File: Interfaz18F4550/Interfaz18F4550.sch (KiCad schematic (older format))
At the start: 13 parts, among them P1 USB-A, U1 LM7805, U2 PIC18F4550, Y1 Crystal_Small

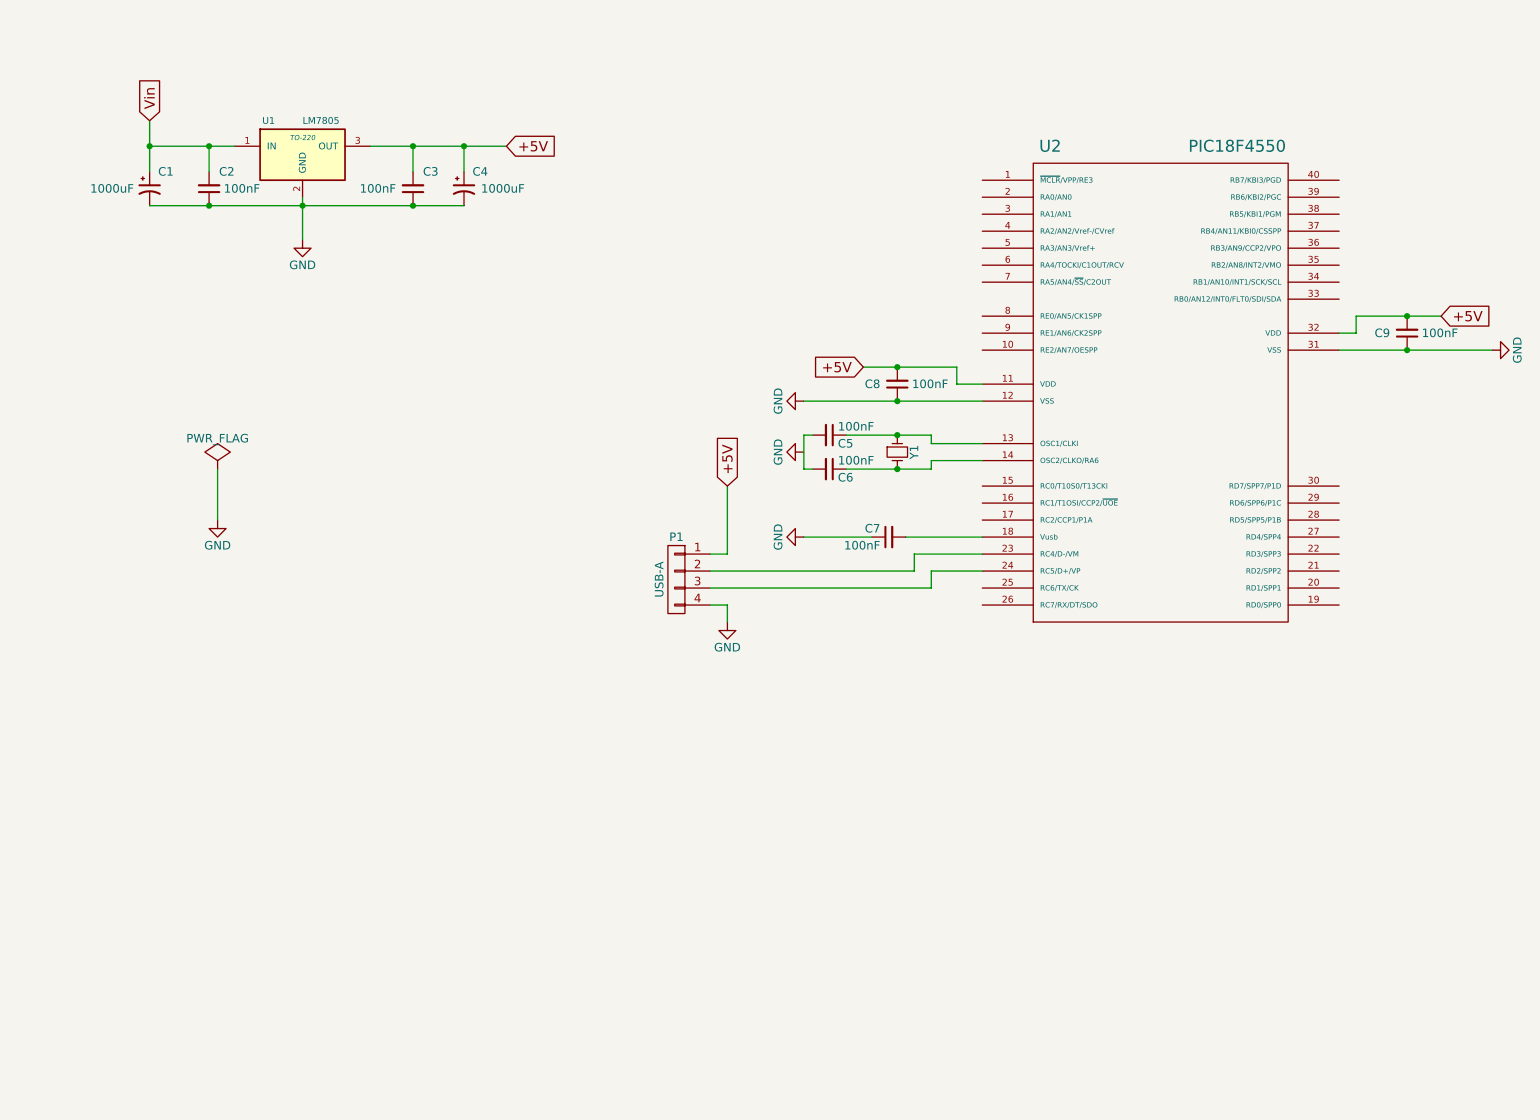
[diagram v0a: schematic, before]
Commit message: Avanzando en interfaz 18f4550
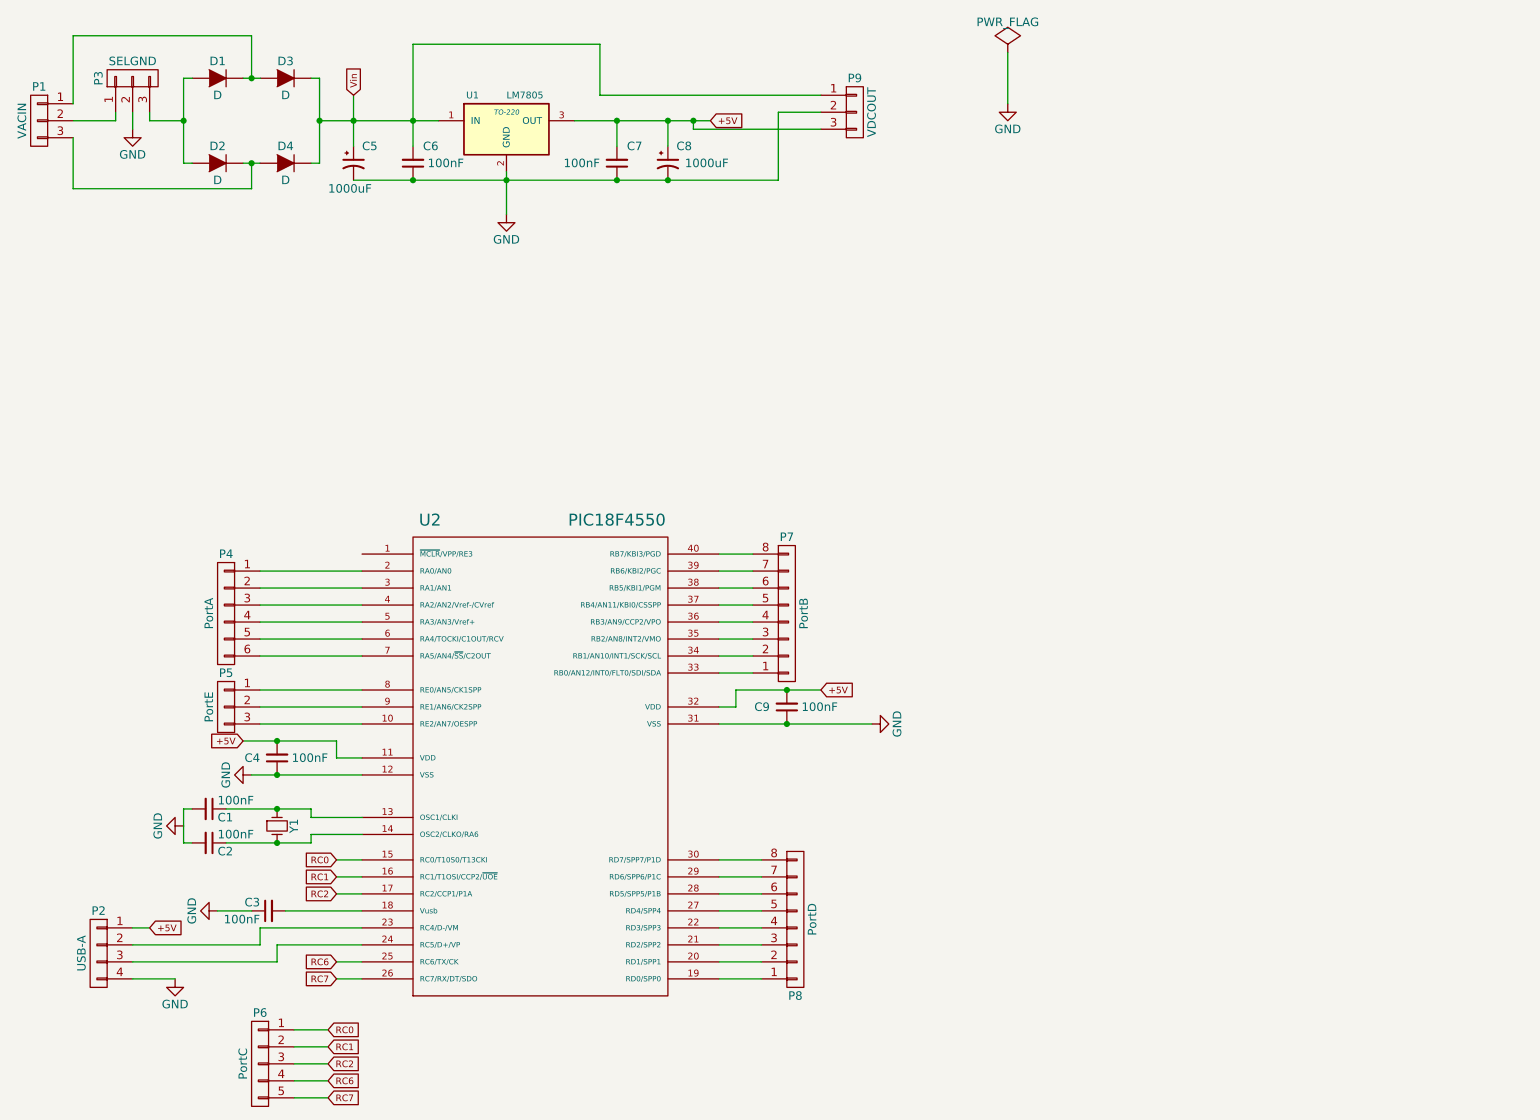
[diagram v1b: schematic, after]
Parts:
- added D1, D2, D3, D4: D, symbol D
- added P1: VACIN, symbol CONN_01X03
- added P3: SELGND, symbol CONN_01X03
- added P4: PortA, symbol CONN_01X06
- added P5: PortE, symbol CONN_01X03
- added P6: PortC, symbol CONN_01X05
- added P7: PortB, symbol CONN_01X08
- added P8: PortD, symbol CONN_01X08
- added P9: VDCOUT, symbol CONN_01X03
- renumbered C5 to C1, C6 to C2, C7 to C3, C8 to C4, C1 to C5, C2 to C6, C3 to C7, C4 to C8, P1 to P2
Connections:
- net +5V: now also P9.3 (P3)
- net GND: now also P3.2 (P2), P9.2 (P2)
- net Vin: now also D3.2 (K), D4.2 (K), P9.1 (P1)
- net at U2.10 (RE2/AN7/OESPP): now also P5.3 (P3)
- net RC0: now reaches U2.15 (RC0/T10S0/T13CKI)
- net RC0: now also P6.1 (P1)
- net RC1: now reaches U2.16 (RC1/T1OSI/CCP2/~UOE~)
- net RC1: now also P6.2 (P2)
- net RC2: now reaches U2.17 (RC2/CCP1/P1A)
- net RC2: now also P6.3 (P3)
- net at U2.19 (RD0/SPP0): now also P8.1 (P1)
- net at U2.2 (RA0/AN0): now also P4.1 (P1)
- net at U2.20 (RD1/SPP1): now also P8.2 (P2)
- net at U2.21 (RD2/SPP2): now also P8.3 (P3)
- net at U2.22 (RD3/SPP3): now also P8.4 (P4)
- net RC6: now reaches U2.25 (RC6/TX/CK)
- net RC6: now also P6.4 (P4)
- net RC7: now reaches U2.26 (RC7/RX/DT/SDO)
- net RC7: now also P6.5 (P5)
- net at U2.27 (RD4/SPP4): now also P8.5 (P5)
- net at U2.28 (RD5/SPP5/P1B): now also P8.6 (P6)
- net at U2.29 (RD6/SPP6/P1C): now also P8.7 (P7)
- net at U2.3 (RA1/AN1): now also P4.2 (P2)
- net at U2.30 (RD7/SPP7/P1D): now also P8.8 (P8)
- net at U2.33 (RB0/AN12/INT0/FLT0/SDI/SDA): now also P7.1 (P1)
- net at U2.34 (RB1/AN10/INT1/SCK/SCL): now also P7.2 (P2)
- net at U2.35 (RB2/AN8/INT2/VMO): now also P7.3 (P3)
- net at U2.36 (RB3/AN9/CCP2/VPO): now also P7.4 (P4)
- net at U2.37 (RB4/AN11/KBI0/CSSPP): now also P7.5 (P5)
- net at U2.38 (RB5/KBI1/PGM): now also P7.6 (P6)
- net at U2.39 (RB6/KBI2/PGC): now also P7.7 (P7)
- net at U2.4 (RA2/AN2/Vref-/CVref): now also P4.3 (P3)
- net at U2.40 (RB7/KBI3/PGD): now also P7.8 (P8)
- net at U2.5 (RA3/AN3/Vref+): now also P4.4 (P4)
- net at U2.6 (RA4/TOCKI/C1OUT/RCV): now also P4.5 (P5)
- net at U2.7 (RA5/AN4/~SS~/C2OUT): now also P4.6 (P6)
- net at U2.8 (RE0/AN5/CK1SPP): now also P5.1 (P1)
- net at U2.9 (RE1/AN6/CK2SPP): now also P5.2 (P2)
- new net: D1.2 (K), D3.1 (A), P1.1 (P1)
- new net: P1.2 (P2), P3.1 (P1)
- new net: D2.2 (K), D4.1 (A), P1.3 (P3)
- new net: D1.1 (A), D2.1 (A), P3.3 (P3)
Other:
- moved on the sheet: C1, C2, C3, C4, C5, C6, C7, C8, C9, P2, U1, U2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

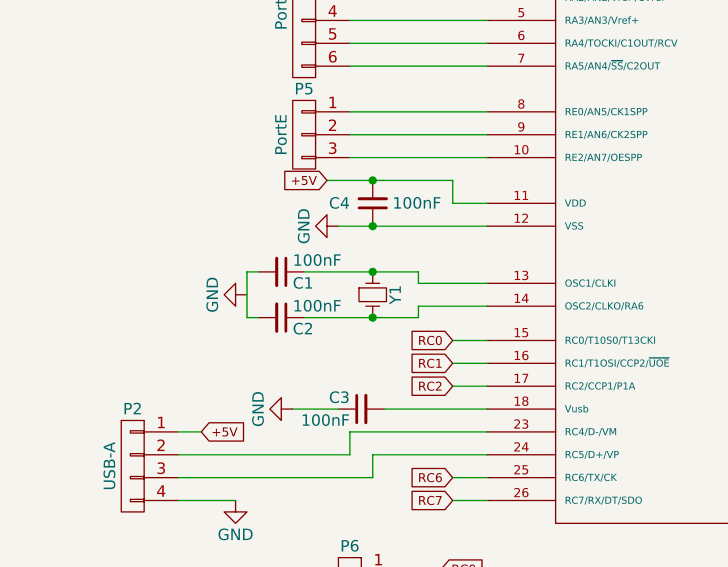
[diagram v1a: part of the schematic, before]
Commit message: Cambios menores en interfaz usb
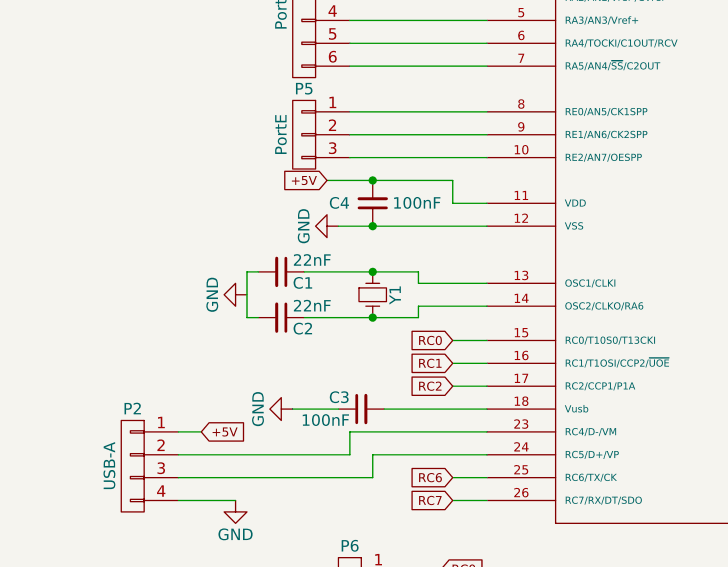
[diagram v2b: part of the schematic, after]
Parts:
- C1, C2: value 100nF -> 22nF
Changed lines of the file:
@@
 LIBS:valves
 LIBS:Kicad-Libreria-Fernando
-LIBS:Interfaz18F4550-cache
+LIBS:Controlador-Temporizador Insoladora-cache
 EELAYER 25 0
 EELAYER END
@@
 P 2150 5300
 F 0 "C1" V 2200 5350 50  0000 L CNN
-F 1 "100nF" V 2100 5350 50  0000 L CNN
+F 1 "22nF" V 2100 5350 50  0000 L CNN
 F 2 "" H 2150 5300 60  0000 C CNN
 F 3 "" H 2150 5300 60  0000 C CNN
@@
 P 2150 5500
 F 0 "C2" V 2200 5550 50  0000 L CNN
-F 1 "100nF" V 2100 5550 50  0000 L CNN
+F 1 "22nF" V 2100 5550 50  0000 L CNN
 F 2 "" H 2150 5500 60  0000 C CNN
 F 3 "" H 2150 5500 60  0000 C CNN
